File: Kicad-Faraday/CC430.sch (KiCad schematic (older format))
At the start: 33 parts, among them P2 DNP, U1 CC430F6137, U14 0915BM15A0001E, X1 ST3215SB32768H5HPWAA, X2 ABM8G-26.000MHZ-18-D2Y-T

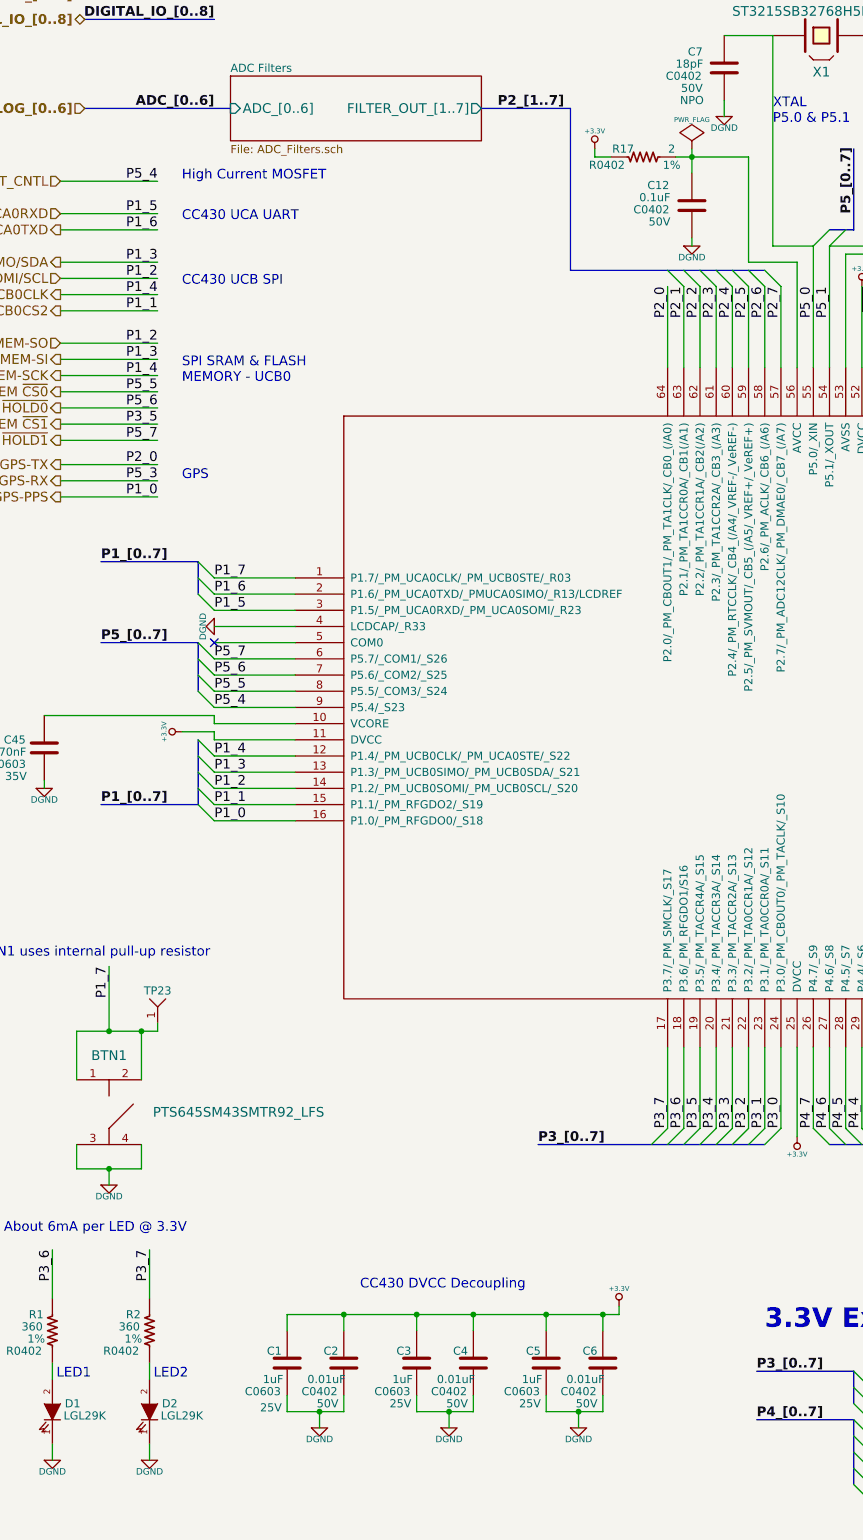
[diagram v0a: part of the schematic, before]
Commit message: Removed basic parts I don't really need to test or am so confident that testing will be fine I'm OK making the changes well in advance
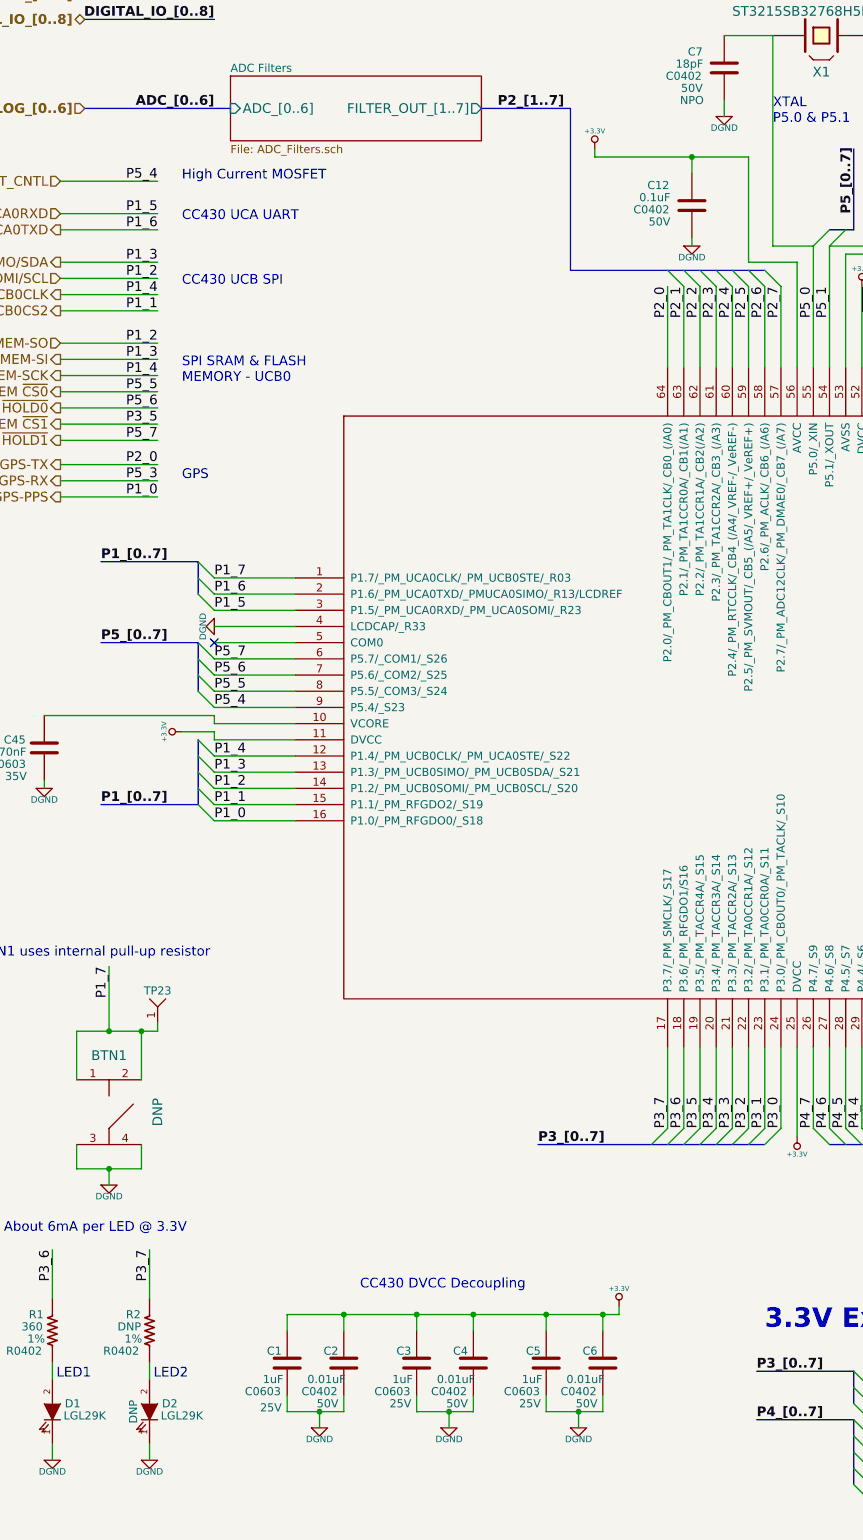
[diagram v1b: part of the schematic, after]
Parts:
- removed R17: 2, R0402, symbol R_US
- BTN1: value PTS645SM43SMTR92_LFS -> DNP
- D2: value LED-IPC -> DNP
- R2: value 360 -> DNP
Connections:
- net +3.3V: now also C12.1, U1.56 (AVCC)
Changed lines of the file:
@@
 Sheet 3 11
 Title "Faraday Wireless Node"
-Date "24 oct 2016"
+Date "2 nov 2016"
 Rev "C"
 Comp "FaradayRF"
@@
 P 1850 9200
 F 0 "R2" H 1750 9300 50  0000 C CNN
-F 1 "360" H 1725 9225 50  0000 C CNN
+F 1 "DNP" H 1725 9225 50  0000 C CNN
 F 2 "R0402" H 1675 9075 50  0000 C CNN
 F 3 "" H 1850 9200 60  0000 C CNN
@@
 P 1600 7850
 F 0 "BTN1" H 1600 8200 60  0000 C CNN
-F 1 "PTS645SM43SMTR92_LFS" H 2400 7850 60  0000 C CNN
+F 1 "DNP" V 1900 7850 60  0000 C CNN
 F 2 "PTS645-SMD" H 1600 7850 60  0001 C CNN
 F 3 "" H 1600 7850 60  0000 C CNN
@@
 	1    0    0    -1
 $EndComp
-$Comp
-L R_US R17
-U 1 1 55BF5F34
-P 4900 1950
-F 0 "R17" V 4950 2075 50  0000 C CNN
-F 1 "2" V 4950 1775 50  0000 C CNN
-F 2 "R0402" V 4850 2175 50  0000 C CNN
-F 3 "" H 4900 1950 60  0000 C CNN
-F 4 "1%" V 4850 1775 50  0000 C CNN "Tolerance"
-	1    4900 1950
-	0    -1   -1   0
-$EndComp
 Text Notes 12450 3700 0    60   ~ 0
 Ferrite Bead
-$Comp
-L PWR_FLAG #FLG048
-U 1 1 55C2C142
-P 5200 1900
-F 0 "#FLG048" H 5200 1995 30  0001 C CNN
-F 1 "PWR_FLAG" H 5200 2080 30  0000 C CNN
-F 2 "" H 5200 1900 60  0000 C CNN
-F 3 "" H 5200 1900 60  0000 C CNN
-	1    5200 1900
-	1    0    0    -1
-$EndComp
 $Bitmap
 Pos 1300 6400
@@
 56 10 04 A1 18 0C 2B 08 82 50 0C 86 15 04 41 28 06 C3 0A 82 20 14 83 61 05 41 10 8A C1 B0 82 20
 08 C5 60 58 41 10 84 62 30 AC 20 08 42 31 FF 0F 83 E1 BA 3C 1C 59 E8 E4 00 00 00 00 49 45 4E 44
-AE 42 60 82 17 $EndBitmap
+AE 42 60 82 D4 $EndBitmap
 EndData
 $EndBitmap
 $Comp
-L DGND #PWR049
+L DGND #PWR048
 U 1 1 55C4A709
 P 2250 4850
-F 0 "#PWR049" H 2250 4850 40  0001 C CNN
+F 0 "#PWR048" H 2250 4850 40  0001 C CNN
 F 1 "DGND" H 2250 4780 40  0000 C CNN
 F 2 "~" H 2250 4850 60  0000 C CNN
@@
 Connection ~ 5200 1950
 Wire Wire Line
-	5100 1950 5550 1950
-Wire Wire Line
-	4600 1950 4700 1950
+	4600 1950 5550 1950
 Wire Wire Line
 	4600 1900 4600 1950
@@
 Wire Wire Line
 	5200 2450 5200 2500
-Wire Wire Line
-	5200 1900 5200 2050
 Connection ~ 1600 7350
 Wire Wire Line
@@
 Connection ~ 10300 1650
 $Comp
-L DGND #PWR050
+L DGND #PWR049
 U 1 1 578D5F78
 P 10300 2550
-F 0 "#PWR050" H 10300 2550 40  0001 C CNN
+F 0 "#PWR049" H 10300 2550 40  0001 C CNN
 F 1 "DGND" H 10300 2480 40  0000 C CNN
 F 2 "~" H 10300 2550 60  0000 C CNN
@@
 	10350 5750 10400 5750
 $Comp
-L DGND #PWR051
+L DGND #PWR050
 U 1 1 57944E95
 P 11700 6350
-F 0 "#PWR051" H 11700 6350 40  0001 C CNN
+F 0 "#PWR050" H 11700 6350 40  0001 C CNN
 F 1 "DGND" H 11700 6280 40  0000 C CNN
 F 2 "~" H 11700 6350 60  0000 C CNN
@@
 P 1850 9700
 F 0 "D2" V 1800 9825 50  0000 C CNN
-F 1 "LED-IPC" H 1850 9600 50  0001 C CNN
+F 1 "DNP" H 1850 9600 50  0000 C CNN
 F 2 "LGL29K" V 1875 9900 50  0000 C CNN
 F 3 "~" H 1850 9700 60  0000 C CNN
@@
 Text HLabel 1450 800  0    60   Input ~ 12
 P4_[0..7]
+Wire Wire Line
+	5200 1950 5200 2050
 $EndSCHEMATC
